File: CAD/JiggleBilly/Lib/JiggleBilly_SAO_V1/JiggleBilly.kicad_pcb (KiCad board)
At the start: 2 copper layers, 86.3 x 94.7 mm, 10 parts, among them X1 Badgelife_sao_connector_v169b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

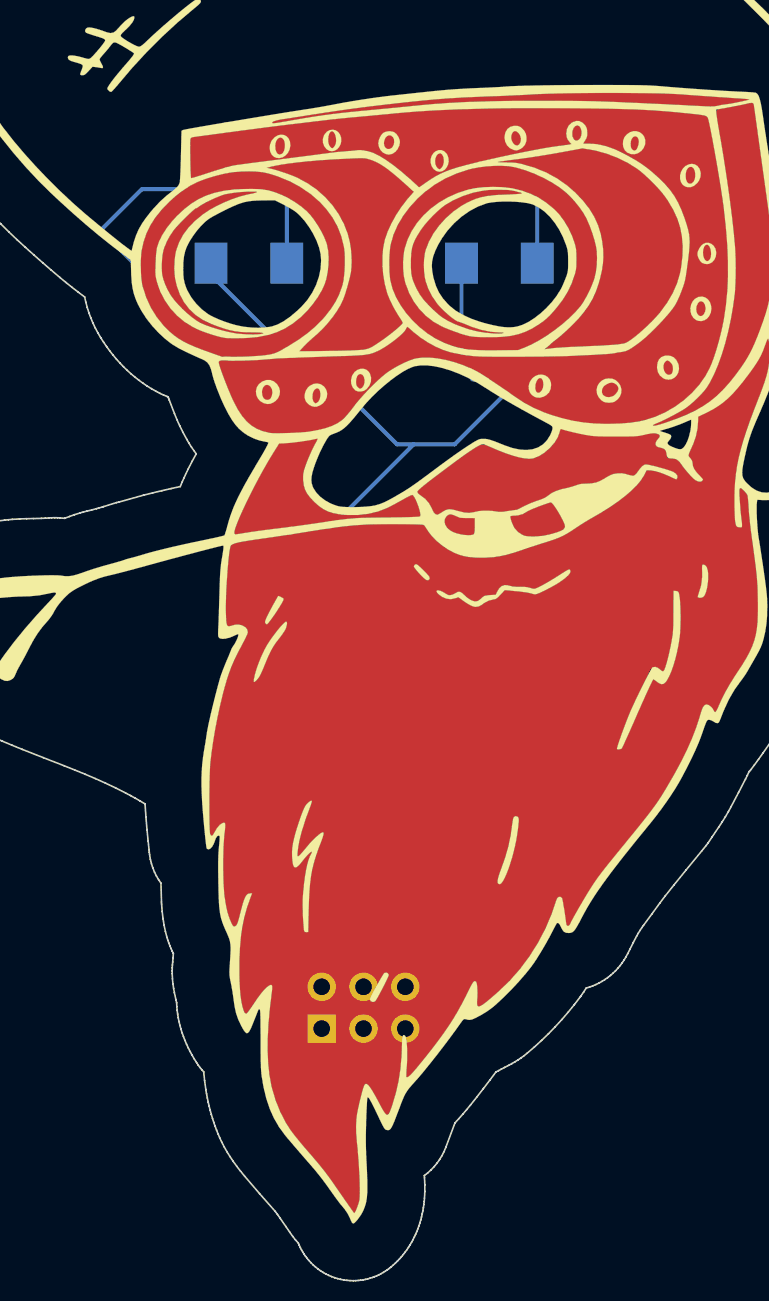
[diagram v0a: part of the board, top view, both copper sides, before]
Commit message: Moved SAO connector and rerouted traces
Moved the SAO connector so it would not conflict with the beard pad
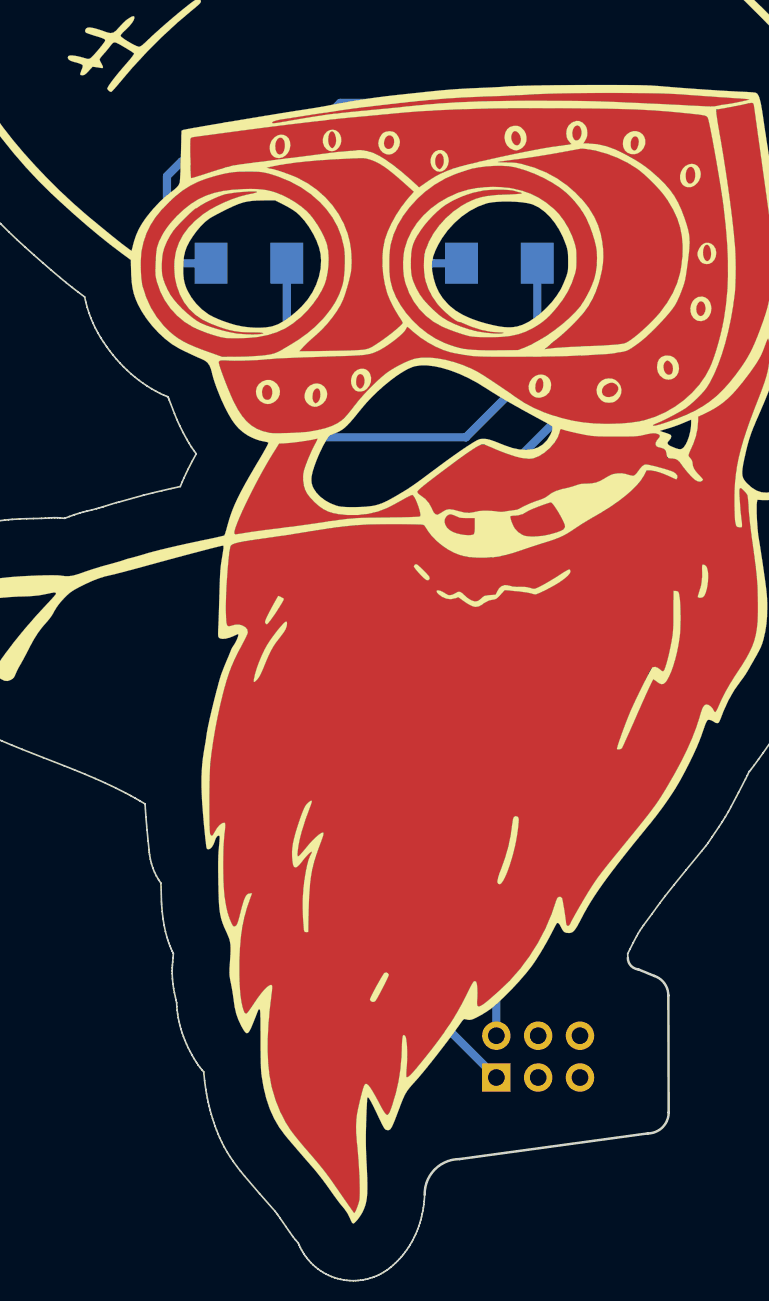
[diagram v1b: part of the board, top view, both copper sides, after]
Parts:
- moved R1 13.2 mm to (102.5, 83.3)
- moved R2 12.9 mm to (113.4, 83.4), turned to 0 degrees
- moved X1 11.0 mm to (118.7, 137.8)
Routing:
- net +3.3V: track 50.7 -> 81.1 mm
- net GND: track 90.6 -> 78.0 mm
- net Net-(D2-A): track 8.90 -> 13.1 mm
- net Net-(D3-A): track 6.95 -> 9.10 mm
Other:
- outline, holes or cut-outs redrawn

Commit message: Update part info
Updated part info for BOM generaton
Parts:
- R1, R2: value 60 -> 90.9
